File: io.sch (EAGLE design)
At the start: 34 parts, among them J1 SJ-3523-SMT-TR, Q1 MMBT2222A-7-FSOT-23_DIO-M, Q2 2SCR574D3TL1TRANS_2SCR573_TO-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, U1 MCP1703T-5002E, U3 LM386M-1

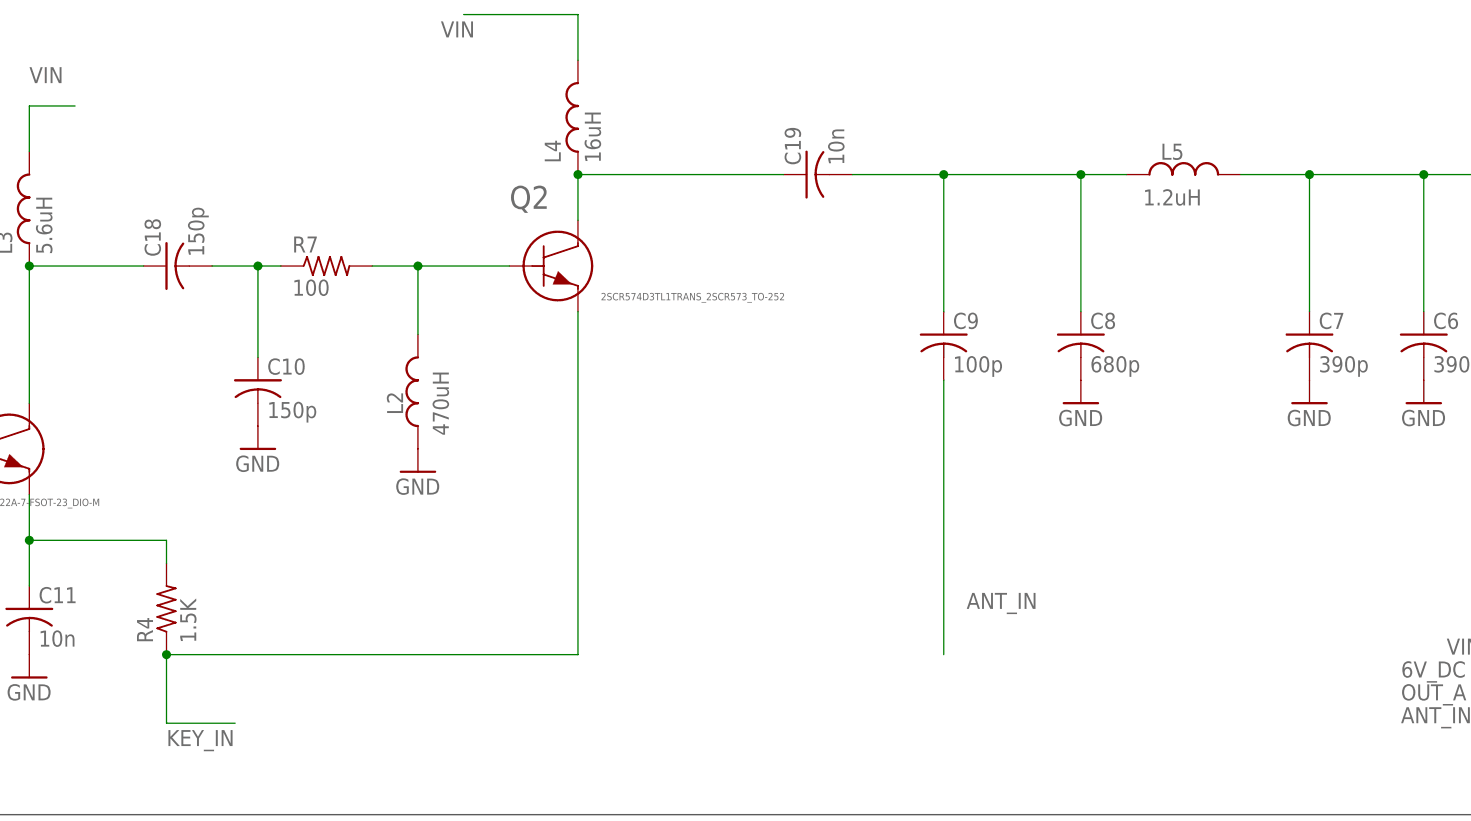
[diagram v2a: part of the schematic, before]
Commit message: v1.3
* replaced L5 and C19 with larger devices capable of more current
* replaced Q2 with another 2222A
* increased power and output wire size to 15mil (from 12)

Revisions based on testing with my amplifier circuit breakout
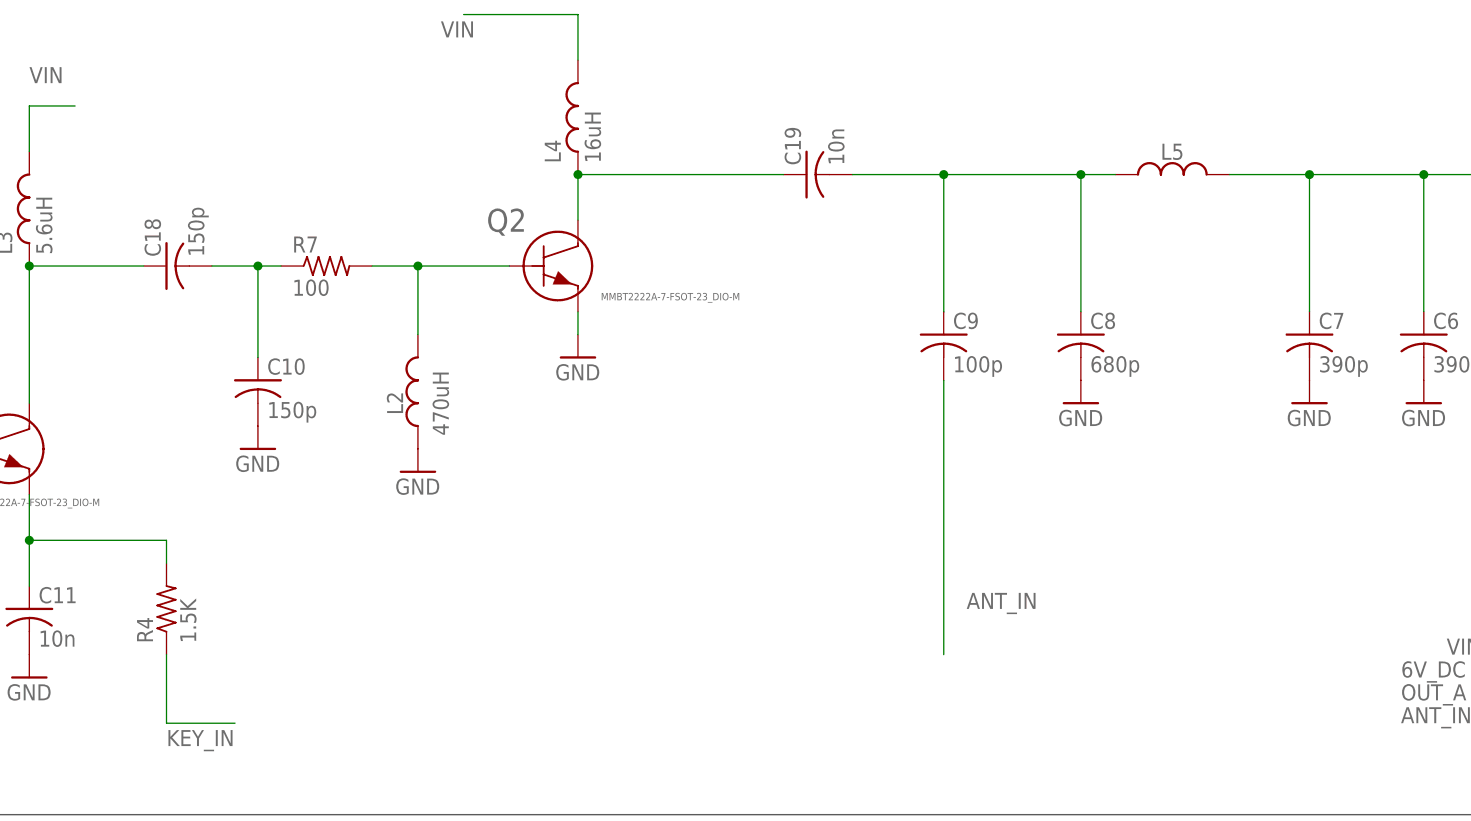
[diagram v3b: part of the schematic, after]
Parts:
- C19: device adafruit:C-USC0805 -> adafruit:C-USC1206
- L5: device Inductor:L_CHIP-0805(2012-METRIC) -> zort2:SRN4018TA-1R2M
- Q2: value 2SCR574D3TL1TRANS_2SCR573_TO-252 -> MMBT2222A-7-FSOT-23_DIO-M; device zort2:2SCR574D3TL1TRANS_2SCR573_TO-252 -> zort2:MMBT2222A-7-FSOT-23_DIO-M
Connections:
- new net N$29: Q2.3
- net KEY_IN: no longer Q2.3
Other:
- moved on the sheet: L5
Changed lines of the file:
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@@
 <class number="0" name="default" width="0" drill="0">
 </class>
-<class number="1" name="power" width="0.3048" drill="0">
+<class number="1" name="power" width="0.381" drill="0">
 </class>
 </classes>
@@
 <part name="C6" library="adafruit" library_urn="urn:adsk.eagle:library:420" deviceset="C-US" device="C0805" package3d_urn="urn:adsk.eagle:package:6240337/1" value="390p"/>
 <part name="C18" library="adafruit" library_urn="urn:adsk.eagle:library:420" deviceset="C-US" device="C0805" package3d_urn="urn:adsk.eagle:package:6240337/1" value="150p"/>
-<part name="C19" library="adafruit" library_urn="urn:adsk.eagle:library:420" deviceset="C-US" device="C0805" package3d_urn="urn:adsk.eagle:package:6240337/1" value="10n"/>
+<part name="C19" library="adafruit" library_urn="urn:adsk.eagle:library:420" deviceset="C-US" device="C1206" package3d_urn="urn:adsk.eagle:package:6240335/1" value="10n"/>
 <part name="R4" library="adafruit" library_urn="urn:adsk.eagle:library:420" deviceset="R-US_" device="M0805" package3d_urn="urn:adsk.eagle:package:6240587/1" value="1.5K"/>
 <part name="R5" library="adafruit" library_urn="urn:adsk.eagle:library:420" deviceset="R-US_" device="M0805" package3d_urn="urn:adsk.eagle:package:6240587/1" value="6.8K"/>
@@
 <part name="GND24" library="supply1" library_urn="urn:adsk.eagle:library:371" deviceset="GND" device=""/>
 <part name="JP1" library="adafruit" library_urn="urn:adsk.eagle:library:420" deviceset="PINHD-2X4" device="" package3d_urn="urn:adsk.eagle:package:6240893/1"/>
-<part name="L5" library="Inductor" library_urn="urn:adsk.eagle:library:16378440" deviceset="L" device="CHIP-0805(2012-METRIC)" package3d_urn="urn:adsk.eagle:package:16378480/1" technology="_" value="1.2uH"/>
+<part name="L5" library="zort2" deviceset="SRN4018TA-1R2M" device="" value="1.2uH"/>
 <part name="L4" library="zort2" deviceset="ASPI-0630LR" device="" value="16uH"/>
 <part name="U$1" library="zort2" deviceset="9V_968" device="9V_968_SMD"/>
-<part name="Q2" library="zort2" deviceset="2SCR574D3TL1" device="TRANS_2SCR573_TO-252"/>
 <part name="L2" library="zort2" deviceset="L" device="CHIP-1008(2520-METRIC)" package3d_urn="urn:adsk.eagle:package:16378469/1" technology="_" value="470uH"/>
 <part name="J1" library="SJ-3523-SMT-TR" deviceset="SJ-3523-SMT-TR" device=""/>
 <part name="ANT" library="zort2" deviceset="SMACONNECTOR" device="_EDGE" package3d_urn="urn:adsk.eagle:package:6240945/1"/>
 <part name="Q1" library="zort2" deviceset="MMBT2222A-7-F" device="SOT-23_DIO-M"/>
+<part name="GND3" library="supply1" library_urn="urn:adsk.eagle:library:371" deviceset="GND" device=""/>
+<part name="Q2" library="zort2" deviceset="MMBT2222A-7-F" device="SOT-23_DIO-M"/>
 </parts>
 <sheets>
@@
 <instance part="L5" gate="G$1" x="109.22" y="10.16" smashed="yes">
 <attribute name="NAME" x="109.22" y="12.7" size="1.778" layer="95" align="center"/>
-<attribute name="VALUE" x="109.22" y="7.62" size="1.778" layer="96" align="center"/>
 </instance>
 <instance part="L4" gate="G$1" x="43.18" y="16.51" smashed="yes" rot="R90">
@@
 </instance>
 <instance part="U$1" gate="G$1" x="-78.74" y="88.9" smashed="yes"/>
-<instance part="Q2" gate="A" x="40.64" y="0" smashed="yes">
-<attribute name="NAME" x="35.56" y="6.35" size="2.54" layer="95" ratio="10" rot="SR0"/>
-<attribute name="VALUE" x="45.72" y="-3.81" size="0.8128" layer="96" ratio="10" rot="SR0"/>
-</instance>
 <instance part="L2" gate="G$1" x="25.4" y="-15.24" smashed="yes" rot="R90">
 <attribute name="NAME" x="22.86" y="-15.24" size="1.778" layer="95" rot="R90" align="center"/>
@@
 <attribute name="NAME" x="-25.4" y="-13.97" size="2.54" layer="95" ratio="10" rot="SR0"/>
 <attribute name="VALUE" x="-25.4" y="-26.67" size="0.8128" layer="96" ratio="10" rot="SR0"/>
+</instance>
+<instance part="GND3" gate="1" x="43.18" y="-10.16" smashed="yes">
+<attribute name="VALUE" x="40.64" y="-12.7" size="1.778" layer="96"/>
+</instance>
+<instance part="Q2" gate="G$1" x="40.64" y="0" smashed="yes">
+<attribute name="NAME" x="33.02" y="3.81" size="2.54" layer="95" ratio="10" rot="SR0"/>
+<attribute name="VALUE" x="45.72" y="-3.81" size="0.8128" layer="96" ratio="10" rot="SR0"/>
 </instance>
 </instances>
@@
 </segment>
 </net>
-<net name="KEY_IN" class="1">
+<net name="KEY_IN" class="0">
 <segment>
 <label x="154.94" y="73.66" size="1.778" layer="95" rot="R270"/>
@@
 <pinref part="R4" gate="G$1" pin="1"/>
 <wire x1="-2.54" y1="-43.18" x2="-2.54" y2="-50.8" width="0.1524" layer="91"/>
+<wire x1="-2.54" y1="-50.8" x2="5.08" y2="-50.8" width="0.1524" layer="91"/>
 <label x="-2.54" y="-53.34" size="1.778" layer="95"/>
-<wire x1="-2.54" y1="-50.8" x2="5.08" y2="-50.8" width="0.1524" layer="91"/>
-<pinref part="Q2" gate="A" pin="3"/>
-<wire x1="-2.54" y1="-43.18" x2="43.18" y2="-43.18" width="0.1524" layer="91"/>
-<wire x1="43.18" y1="-43.18" x2="43.18" y2="-5.08" width="0.1524" layer="91"/>
-<junction x="-2.54" y="-43.18"/>
 </segment>
 </net>
@@
 <wire x1="25.4" y1="0" x2="35.56" y2="0" width="0.1524" layer="91"/>
 <junction x="25.4" y="0"/>
-<pinref part="Q2" gate="A" pin="1"/>
 <pinref part="L2" gate="G$1" pin="2"/>
+<pinref part="Q2" gate="G$1" pin="1"/>
 </segment>
 </net>
@@
 <pinref part="L4" gate="G$1" pin="1"/>
 <junction x="43.18" y="10.16"/>
-<pinref part="Q2" gate="A" pin="2"/>
+<pinref part="Q2" gate="G$1" pin="2"/>
 </segment>
 </net>
@@
 <pinref part="C8" gate="G$1" pin="1"/>
 <wire x1="99.06" y1="10.16" x2="99.06" y2="-5.08" width="0.1524" layer="91"/>
-<wire x1="104.14" y1="10.16" x2="99.06" y2="10.16" width="0.1524" layer="91"/>
+<wire x1="102.87" y1="10.16" x2="99.06" y2="10.16" width="0.1524" layer="91"/>
 <junction x="99.06" y="10.16"/>
 <pinref part="L5" gate="G$1" pin="1"/>
@@
 <net name="N$26" class="1">
 <segment>
-<wire x1="116.84" y1="10.16" x2="124.46" y2="10.16" width="0.1524" layer="91"/>
+<wire x1="115.57" y1="10.16" x2="124.46" y2="10.16" width="0.1524" layer="91"/>
 <pinref part="C7" gate="G$1" pin="1"/>
 <wire x1="124.46" y1="10.16" x2="124.46" y2="-5.08" width="0.1524" layer="91"/>
@@
 </segment>
 </net>
+<net name="N$29" class="1">
+<segment>
+<wire x1="43.18" y1="-7.62" x2="43.18" y2="-5.08" width="0.1524" layer="91"/>
+<pinref part="GND3" gate="1" pin="GND"/>
+<pinref part="Q2" gate="G$1" pin="3"/>
+</segment>
+</net>
